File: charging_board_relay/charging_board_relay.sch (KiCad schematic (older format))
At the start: 71 parts

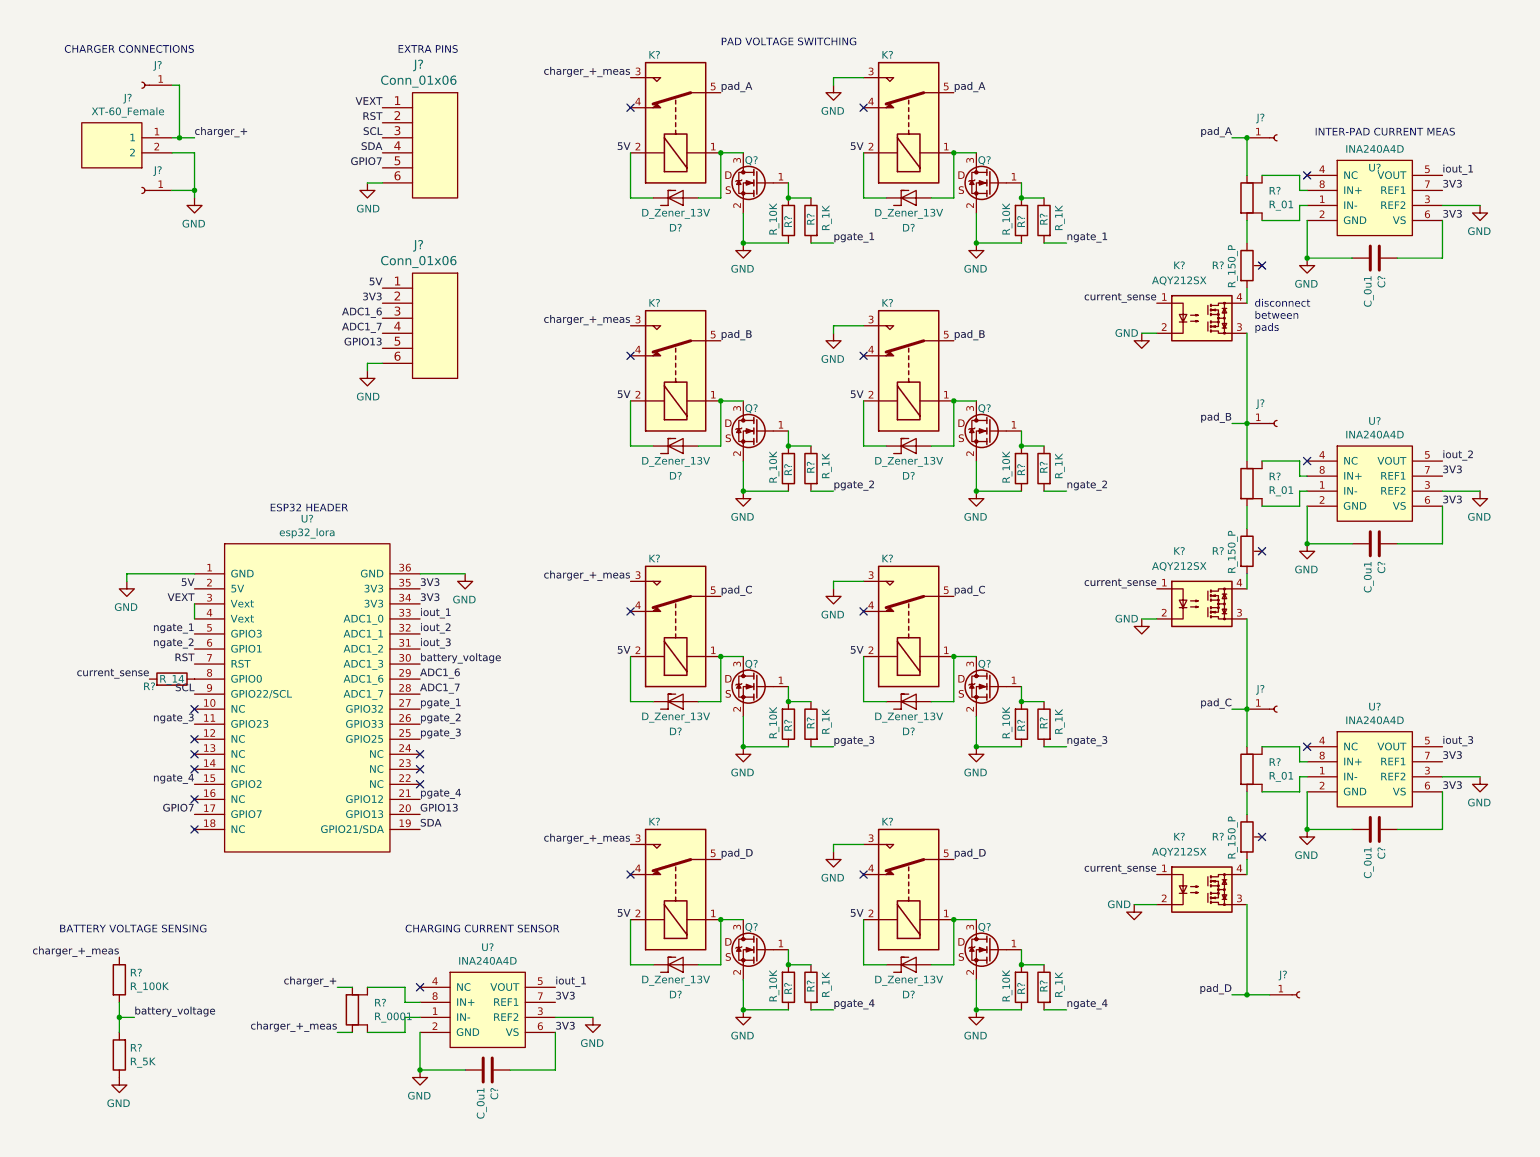
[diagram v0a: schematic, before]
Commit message: finalized charging board design
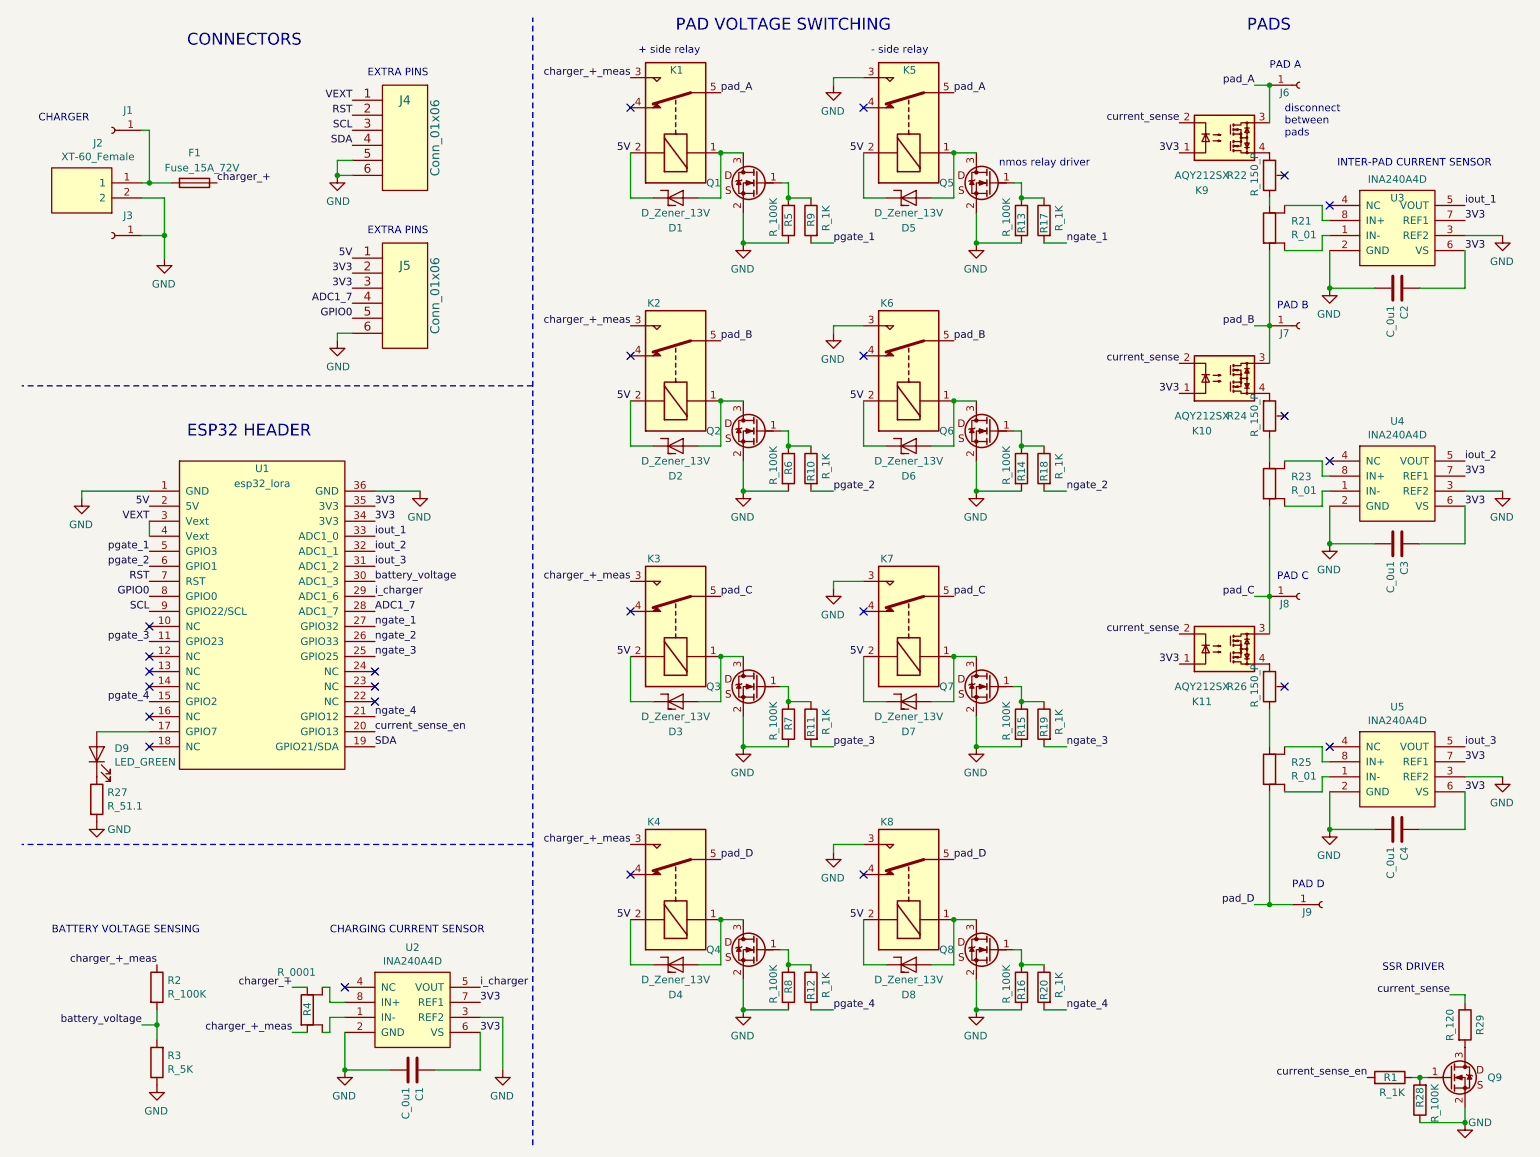
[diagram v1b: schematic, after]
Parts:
- removed D? (x8): D_Zener_13V, footprints:D_13V_Zener, symbol rocketry:D_Zener_13V
- removed Q? (x8): TN2404K-T1-GE3, personal:SOT-23, symbol personal:TN2404K-T1-GE3
- removed R? (x8): R_10K, personal:R_0805, symbol personal:R_10K
- removed R?: R_14, personal:R_0805, symbol personal:R_14
- added D1, D2, D3, D4, D5, D6, D7, D8: D_Zener_13V, personal:1SMB5928BT3G, symbol personal:D_Zener_13V
- added D9: LED_GREEN, LEDs:LED_0603_HandSoldering, symbol personal:LED_GREEN
- added F1: Fuse_15A_72V, personal:0697H9200-01, symbol personal:Fuse_15A_72V
- added Q1, Q2, Q3, Q4, Q5, Q6, Q7, Q8, Q9: NVS4409NT1G, TO_SOT_Packages_SMD:SOT-323_SC-70, symbol personal:NVS4409NT1G
- added R1: R_1K, personal:R_0805, symbol personal:R_1K
- added R13, R14, R15, R16, R28, R5, R6, R7, R8: R_100K, personal:R_0805, symbol personal:R_100K
- added R27: R_51.1, personal:R_0805, symbol personal:R_51.1
- added R29: R_120, personal:R_0805, symbol personal:R_120
- J6, J7, J8, J9: renamed from J?; footprint personal:power_pin_01x01 -> personal:power_pin_01x02
- K1, K2, K3, K4, K5, K6, K7, K8: renamed from K?; footprint footprints:Relay_SPDT_OMRON-G2RL-1-E -> personal:OMIH-SH-105L,394
- R22, R24, R26: renamed from R?; DPN 311-10.0CRCT-ND -> PWR263S-20-1500JECT-ND
- R3: renamed from R?; DPN 311-1.0KARCT-ND -> 311-4.99CRCT-ND
- R4: renamed from R?; DPN 311-1.0KARCT-ND -> 2037-RL1632T4F-R001-FNHCT-ND
- gave numbers to parts that had none: 29
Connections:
- net 3V3: now also J5.3, K10.1, K11.1, K9.1
- net 5V: now also D1.1 (K), D2.1 (K), D3.1 (K), D4.1 (K), D5.1 (K), D6.1 (K), D7.1 (K), D8.1 (K)
- net GND: now also J4.5, Q1.2, Q2.2, Q3.2, Q4.2, Q5.2, Q6.2, Q7.2, Q8.2, Q9.2, R13.2, R14.2, R15.2, R16.2, R27.2, R28.1, R5.2, R6.2, R7.2, R8.2; no longer K10.2, K11.2, K9.2
- net charger_+: now also R4.1, F1.1; no longer J1.1 (Pin_1), J2.1, R4.2
- net charger_+_meas: now also R4.2; no longer R4.1
- net current_sense: now also K10.2, K11.2, K9.2, R29.1; no longer K10.1, K11.1, K9.1
- net iout_1: no longer U2.5 (VOUT)
- net ngate_1: now also U1.27 (GPIO32); no longer U1.5 (GPIO3)
- net ngate_2: now also U1.26 (GPIO33); no longer U1.6 (GPIO1)
- net ngate_3: now also U1.25 (GPIO25); no longer U1.11 (GPIO23)
- net ngate_4: now also U1.21 (GPIO12); no longer U1.15 (GPIO2)
- net pad_A: now also K9.3; no longer R21.1
- net pad_B: now also K10.3, R21.2; no longer K9.3, R23.1
- net pad_C: now also K11.3, R23.2; no longer K10.3, R25.1
- net pad_D: now also R25.2; no longer K11.3
- net pgate_1: now also U1.5 (GPIO3); no longer U1.27 (GPIO32)
- net pgate_2: now also U1.6 (GPIO1); no longer U1.26 (GPIO33)
- net pgate_3: now also U1.11 (GPIO23); no longer U1.25 (GPIO25)
- net pgate_4: now also U1.15 (GPIO2); no longer U1.21 (GPIO12)
- net GPIO0: now reaches U1.8 (GPIO0)
- net GPIO0: now also J5.5
- net at R22.1: now also R21.1; no longer R21.2
- net at K2.1: now also D2.2 (A), Q2.3
- net at R10.1: now also Q2.1, R6.1
- net at K6.1: now also D6.2 (A), Q6.3
- net at R18.1: now also Q6.1, R14.1
- net at U2.1 (IN-): now also R4.4; no longer R4.3
- net at U2.8 (IN+): now also R4.3; no longer R4.4
- net at K3.1: now also D3.2 (A), Q3.3
- net at R11.1: now also Q3.1, R7.1
- net at K7.1: now also D7.2 (A), Q7.3
- net at R19.1: now also Q7.1, R15.1
- net at K4.1: now also D4.2 (A), Q4.3
- net at R12.1: now also Q4.1, R8.1
- net at K8.1: now also D8.2 (A), Q8.3
- net at R20.1: now also Q8.1, R16.1
- net at R24.1: now also R23.1; no longer R23.2
- net at R26.1: now also R25.1; no longer R25.2
- net at K1.1: now also D1.2 (A), Q1.3
- net at K5.1: now also D5.2 (A), Q5.3
- net at R9.1: now also Q1.1, R5.1
- net at R17.1: now also Q5.1, R13.1
- net ADC1_6 renamed i_charger
- net i_charger: now also U2.5 (VOUT); no longer J5.3
- net GPIO13 renamed current_sense_en
- net current_sense_en: now also R1.2; no longer J5.5
- net GPIO7: no longer names the net of U1.17 (GPIO7)
- net GPIO7: now also D9.2 (A); no longer J4.5
- new net: D9.1 (K), R27.1
- new net: F1.2, J1.1 (Pin_1), J2.1
- new net: Q9.3, R29.2
- new net: Q9.1, R1.1, R28.2
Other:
- note added: "+ side relay"
- note added: "- side relay"
- note added: "CHARGER"
- note added: "CONNECTORS"
- note added: "INTER-PAD CURRENT SENSOR\n"
- note added: "PAD A"
- note added: "PAD B"
- note added: "PAD C"
- note added: "PAD D"
- note added: "PADS"
- note added: "SSR DRIVER"
- note added: "nmos relay driver\n"
- note removed: "CHARGER CONNECTIONS"
- note removed: "INTER-PAD CURRENT MEAS\n"
- moved on the sheet: C1, C2, C3, C4, J1, J2, J3, J4, J5, J6, J7, J8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
